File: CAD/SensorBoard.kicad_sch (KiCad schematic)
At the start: 69 parts, among them J1 USB C 2.0, J2 ARM SWD TagConnect, SW1 BOOT_SW, SW2 BOOT_SW, SW3 BOOT_SW, SW4 BOOT_SW, SW5 BOOT_SW, U1 STM32U073CCT6, U2 BME680, U3 BMI323, U4 TC1047, U5 USBLC6-2SC6, U6 MIC5365-3.3YD5, X1 32MHz, X2 32kHz768

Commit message: Add external connectors
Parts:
- removed J2: ARM SWD TagConnect, Connector:Tag-Connect_TC2030-IDC-FP_2x03_P1.27mm_Vertical, symbol Connector:Conn_ARM_SWD_TagConnect_TC2030
- removed U3: BMI323, SensorBoard:BMI323, symbol SensorBoard:BMI323
- added C20: 100n, symbol Device:C
- added J2: Conn_SWD, symbol SensorBoard:Conn_SWD
- added J3: Conn_UART, symbol SensorBoard:Conn_UART
- added J4: Conn_DAC, symbol SensorBoard:Conn_DAC
- added R26: 220, symbol Device:R
- added R27, R28, R29, R30: 100, symbol Device:R
- added SW6: BOOT_SW, symbol Switch:SW_Push
- added U5: BMI323, SensorBoard:BMI323, symbol SensorBoard:BMI323
- renumbered C11 to C1, C8 to C10, C22 to C11, C1 to C12, C2 to C13, C3 to C14, C4 to C15, C5 to C16, C6 to C17, C16 to C18, C15 to C19, C12 to C2, C14 to C21, C18 to C22, C17 to C23, C13 to C3, C19 to C4, C20 to C5, C21 to C6, C9 to C7, C10 to C8, C7 to C9, D3 to D1, D4 to D2, D5 to D3, D1 to D4, D2 to D5, R8 to R1, R16 to R10, R17 to R11, R4 to R12, R5 to R13, R18 to R14, R19 to R15, R20 to R16, R21 to R17, R1 to R18, R22 to R19, R3 to R2, R23 to R20, R24 to R21, R25 to R22, R12 to R23, R13 to R24, R11 to R25, R10 to R3, R9 to R4, R2 to R5, R7 to R6, R6 to R7, R14 to R8, R15 to R9, U5 to U1, U6 to U2, U2 to U3, U1 to U6
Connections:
- net +3V3: now also U5.5 (VDDIO), U5.8 (VDD)
- net DAC_OUT: now also J4.1 (DAC_OUT)
- net GND: now also C20.1, J2.3 (GND), J2.4 (SHIELD), J3.3 (GND), J3.4 (SHIELD), J4.2 (GND), J4.3 (SHIELD), SW6.1, U5.6 (GNDIO), U5.7 (GND)
- net IMU_INT1: now also U5.4 (INT1)
- net IMU_INT2: now also U5.9 (INT2)
- net SPI_MISO: now also U5.1 (SDO)
- net SPI_MOSI: now also U5.14 (SDX)
- net SPI_NCS: now also U5.12 (~{CSB})
- net SPI_SCK: now also U5.13 (SCX)
- net SWD_SWCLK: now also J2.1 (SWDCLK), R30.2; no longer U6.37 (PA14)
- net UART_RX: now also J3.2 (RX), R28.1; no longer U6.22 (PB11)
- net UART_TX: now also J3.1 (TX), R27.1; no longer U6.21 (PB10)
- net SWD_DWDIO renamed SWD_SWDIO_R
- net SWD_SWDIO_R: now also R29.1
- net SWD_RST renamed MCU_RST
- net MCU_RST: now also C20.2, R26.2
- net SWD_SWO: no longer names the net of U6.39 (PB3)
- new net: R26.1, SW6.2
- new net SWD_SWCLK_R: R30.1, U6.37 (PA14)
- new net SWD_SWDIO: J2.2 (SWDIO), R29.2
- new net UART_RX_R: R28.2, U6.22 (PB11)
- new net UART_TX_R: R27.2, U6.21 (PB10)
- no-connect marks 5 -> 6
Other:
- note added: "SDO (ADDR_SEL) connected to GND => I2C Address: 0x76"
- note added: "~{CSB} (PROT_SEL) connected to +3V3 => I2C Selected"
- moved on the sheet: C11, C21, C22, C23, C4, C5, C6, R14, R15, R16, R17, R19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

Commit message: Schematic clean-up
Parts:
- removed R25: 22, symbol Device:R
- added C1: 4u7, Capacitor_SMD:C_0603_1608Metric, symbol Device:C
- C10: renamed from C7; footprint (none) -> Capacitor_SMD:C_0402_1005Metric
- C11: renamed from C8; footprint (none) -> Capacitor_SMD:C_0402_1005Metric
- C12: renamed from C9; footprint (none) -> Capacitor_SMD:C_0402_1005Metric
- C13: renamed from C10; footprint (none) -> Capacitor_SMD:C_0402_1005Metric
- C14: renamed from C1; footprint (none) -> Capacitor_SMD:C_0402_1005Metric
- C15: renamed from C20; footprint (none) -> Capacitor_SMD:C_0402_1005Metric
- C16: renamed from C4; footprint (none) -> Capacitor_SMD:C_0402_1005Metric
- C17: renamed from C5; footprint (none) -> Capacitor_SMD:C_0402_1005Metric
- C18: renamed from C6; footprint (none) -> Capacitor_SMD:C_0402_1005Metric
- C19: renamed from C11; footprint (none) -> Capacitor_SMD:C_0402_1005Metric
- C2: renamed from C17; footprint (none) -> Capacitor_SMD:C_0603_1608Metric
- C20: renamed from C18; footprint (none) -> Capacitor_SMD:C_0402_1005Metric
- C21: renamed from C19; footprint (none) -> Capacitor_SMD:C_0402_1005Metric
- C22: renamed from C21; footprint (none) -> Capacitor_SMD:C_0402_1005Metric
- C23: renamed from C22; footprint (none) -> Capacitor_SMD:C_0402_1005Metric
- C24: renamed from C23; footprint (none) -> Capacitor_SMD:C_0402_1005Metric
- C3: renamed from C16; footprint (none) -> Capacitor_SMD:C_0402_1005Metric
- C4: renamed from C15; footprint (none) -> Capacitor_SMD:C_0402_1005Metric
- C5: renamed from C14; footprint (none) -> Capacitor_SMD:C_0402_1005Metric
- C6: renamed from C13; footprint (none) -> Capacitor_SMD:C_0402_1005Metric
- C7: renamed from C12; footprint (none) -> Capacitor_SMD:C_0402_1005Metric
- C8: renamed from C2; value 1u -> 4u7; footprint (none) -> Capacitor_SMD:C_0603_1608Metric
- C9: renamed from C3; value 1u -> 4u7; footprint (none) -> Capacitor_SMD:C_0603_1608Metric
- D1: renamed from D2; value LED -> RED; footprint (none) -> LED_SMD:LED_0402_1005Metric
- D2: renamed from D3; value LED -> RED; footprint (none) -> LED_SMD:LED_0402_1005Metric
- D3: renamed from D6; value LED -> RED; footprint (none) -> LED_SMD:LED_0402_1005Metric
- D4: renamed from D7; value LED -> RED; footprint (none) -> LED_SMD:LED_0402_1005Metric
- D6: renamed from D4; footprint (none) -> LED_SMD:LED_0402_1005Metric
- D7: renamed from D5; footprint (none) -> LED_SMD:LED_0402_1005Metric
- J1: footprint (none) -> Connector_USB:USB_C_Receptacle_GCT_USB4105-xx-A_16P_TopMnt_Horizontal
- J2: value Conn_SWD -> SWD Connector; footprint (none) -> Connector_Molex:Molex_PicoBlade_53048-0410_1x04_P1.25mm_Horizontal
- J3: value Conn_UART -> UART Connector; footprint (none) -> Connector_Molex:Molex_PicoBlade_53048-0410_1x04_P1.25mm_Horizontal
- J4: value Conn_DAC -> DAC Connector; footprint (none) -> Connector_Molex:Molex_PicoBlade_53261-0271_1x02-1MP_P1.25mm_Horizontal
- R1: renamed from R23; footprint (none) -> Resistor_SMD:R_0402_1005Metric
- R10: renamed from R7; footprint (none) -> Resistor_SMD:R_0402_1005Metric
- R11: renamed from R18; footprint (none) -> Resistor_SMD:R_0402_1005Metric
- R12: renamed from R2; footprint (none) -> Resistor_SMD:R_0402_1005Metric
- R13: renamed from R5; footprint (none) -> Resistor_SMD:R_0402_1005Metric
- R14: renamed from R26; footprint (none) -> Resistor_SMD:R_0402_1005Metric
- R15: renamed from R14; footprint (none) -> Resistor_SMD:R_0402_1005Metric
- R16: renamed from R15; footprint (none) -> Resistor_SMD:R_0402_1005Metric
- R17: renamed from R16; footprint (none) -> Resistor_SMD:R_0402_1005Metric
- R18: renamed from R17; footprint (none) -> Resistor_SMD:R_0402_1005Metric
- R19, R20, R21, R22: footprint (none) -> Resistor_SMD:R_0402_1005Metric
- R2: renamed from R24; footprint (none) -> Resistor_SMD:R_0402_1005Metric
- R23: renamed from R1; footprint (none) -> Resistor_SMD:R_0402_1005Metric
- R24: renamed from R3; footprint (none) -> Resistor_SMD:R_0402_1005Metric
- R25: renamed from R4; footprint (none) -> Resistor_SMD:R_0402_1005Metric
- R26: renamed from R8; footprint (none) -> Resistor_SMD:R_0402_1005Metric
- R27: renamed from R9; footprint (none) -> Resistor_SMD:R_0402_1005Metric
- R28: renamed from R10; footprint (none) -> Resistor_SMD:R_0402_1005Metric
- R29: renamed from R11; footprint (none) -> Resistor_SMD:R_0402_1005Metric
- R3: renamed from R27; footprint (none) -> Resistor_SMD:R_0402_1005Metric
- R4: renamed from R28; footprint (none) -> Resistor_SMD:R_0402_1005Metric
- R5: renamed from R29; footprint (none) -> Resistor_SMD:R_0402_1005Metric
- R6: renamed from R30; footprint (none) -> Resistor_SMD:R_0402_1005Metric
- R7: renamed from R12; footprint (none) -> Resistor_SMD:R_0402_1005Metric
- R8: renamed from R13; footprint (none) -> Resistor_SMD:R_0402_1005Metric
- R9: renamed from R6; footprint (none) -> Resistor_SMD:R_0402_1005Metric
- SW1: renamed from SW2; value BOOT_SW -> SW_1; footprint (none) -> Button_Switch_SMD:SW_Push_SPST_NO_Alps_SKRK
- SW2: renamed from SW3; value BOOT_SW -> SW_2; footprint (none) -> Button_Switch_SMD:SW_Push_SPST_NO_Alps_SKRK
- SW3: renamed from SW4; value BOOT_SW -> SW_3; footprint (none) -> Button_Switch_SMD:SW_Push_SPST_NO_Alps_SKRK
- SW4: renamed from SW5; value BOOT_SW -> SW_4; footprint (none) -> Button_Switch_SMD:SW_Push_SPST_NO_Alps_SKRK
- SW5: renamed from SW1; value BOOT_SW -> SW_BOOT; footprint (none) -> Button_Switch_SMD:SW_Push_SPST_NO_Alps_SKRK
- SW6: value BOOT_SW -> SW_RST; footprint (none) -> Button_Switch_SMD:SW_Push_SPST_NO_Alps_SKRK
- U2: value MIC5365-3.3YD5 -> MIC5365
- U6: renamed from U4; symbol Sensor_Temperature:TC1047xNB -> SensorBoard:TC1047
- X1: footprint (none) -> Crystal:Crystal_SMD_2016-4Pin_2.0x1.6mm
- X2: footprint (none) -> Crystal:Crystal_SMD_2012-2Pin_2.0x1.2mm
- renumbered D1 to D5, U6 to U1, U1 to U3, U3 to U4
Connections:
- net SPI_SCK_R is gone; now on net SPI_SCK: U1.26 (PB13)
- net +3V3: now also C1.2
- net GND: now also C1.1
- net LED_4_R: now reaches D4.2 (A), R29.2
- net HSE_OUT_R: now reaches C11.1, R11.1, X1.3
- net LED_2_R: now reaches D2.2 (A), R27.2
- net LED_R_R: now reaches D5.5 (AR), R24.2
- net BTN_3_R: now reaches R19.1, SW3.2
- net LED_G_R: now reaches D5.4 (AG), R23.2
- net LED_3_R: now reaches D3.2 (A), R28.2
- net LED_1_R: now reaches D1.2 (A), R26.2
- net MCU_BOOT_R: now reaches R12.1, SW5.2
- net LED_B_R: now reaches D5.6 (AB), R25.2
- net BTN_4_R: now reaches R21.1, SW4.2
- net MCU_RST_R: now reaches R14.1, SW6.2
- net BTN_2_R: now reaches R17.1, SW2.2
- net BTN_1_R: now reaches R15.1, SW1.2
- net BOOT renamed MCU_BOOT
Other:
- note added: "+5V and +3V3 Debug LEDs"
- note added: "Analogue Temperature Sensor"
- note added: "BOOT and ~{RESET} Buttons"
- note added: "External DAC Connector"
- note added: "External SWD Connector"
- note added: "External UART Connector"
- note added: "High-Speed External Crystal Oscillatror (32MHz)"
- note added: "Humidity, Pressure, Temperature, and Volatile Organic Compounds Sensor on I^{2}C"
- note added: "Inertial Measurement Unit on SPI"
- note added: "Low-Speed External Crystal Oscillatror (32Hz768)"
- note added: "RGB and 4 Red LEDs"
- note added: "SDO (ADDR_SEL) connected to GND => I^{2}C Address: 0x76"
- note added: "USB Type-C 2.0 Connector with ESD Protection"
- note added: "Ultra-Low Power Microcontroller - STM32U073"
- note added: "User buttons"
- note added: "~{CSB} (PROT_SEL) connected to +3V3 => I^{2}C Selected"
- note removed: "SDO (ADDR_SEL) connected to GND => I2C Address: 0x76"
- note removed: "~{CSB} (PROT_SEL) connected to +3V3 => I2C Selected"
- moved on the sheet: C10, C11, C12, C13, C14, C15, C16, C17, C18, C19, C2, C20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

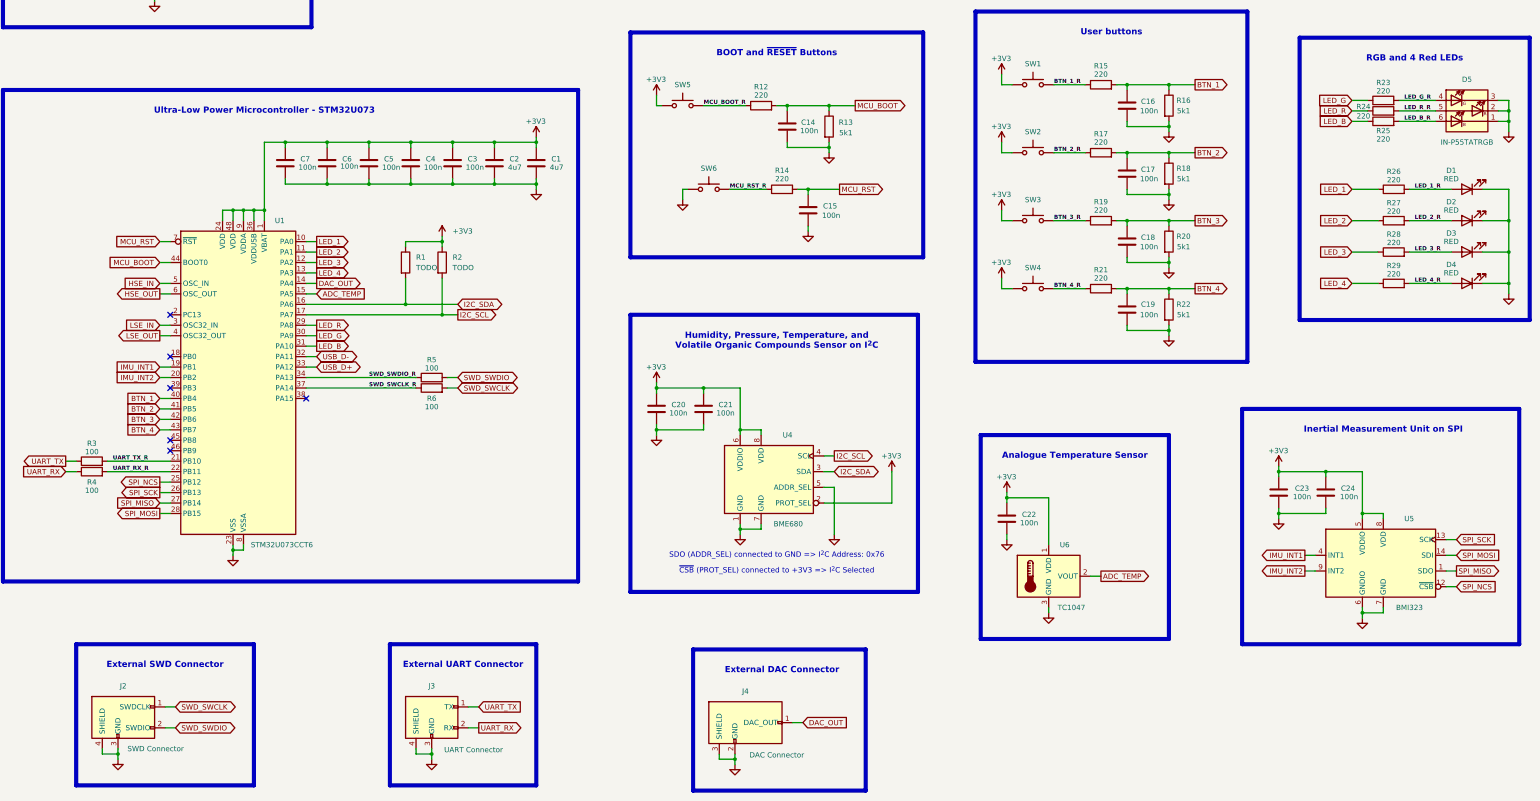
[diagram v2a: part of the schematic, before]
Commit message: Update connector footprints and RGB LED
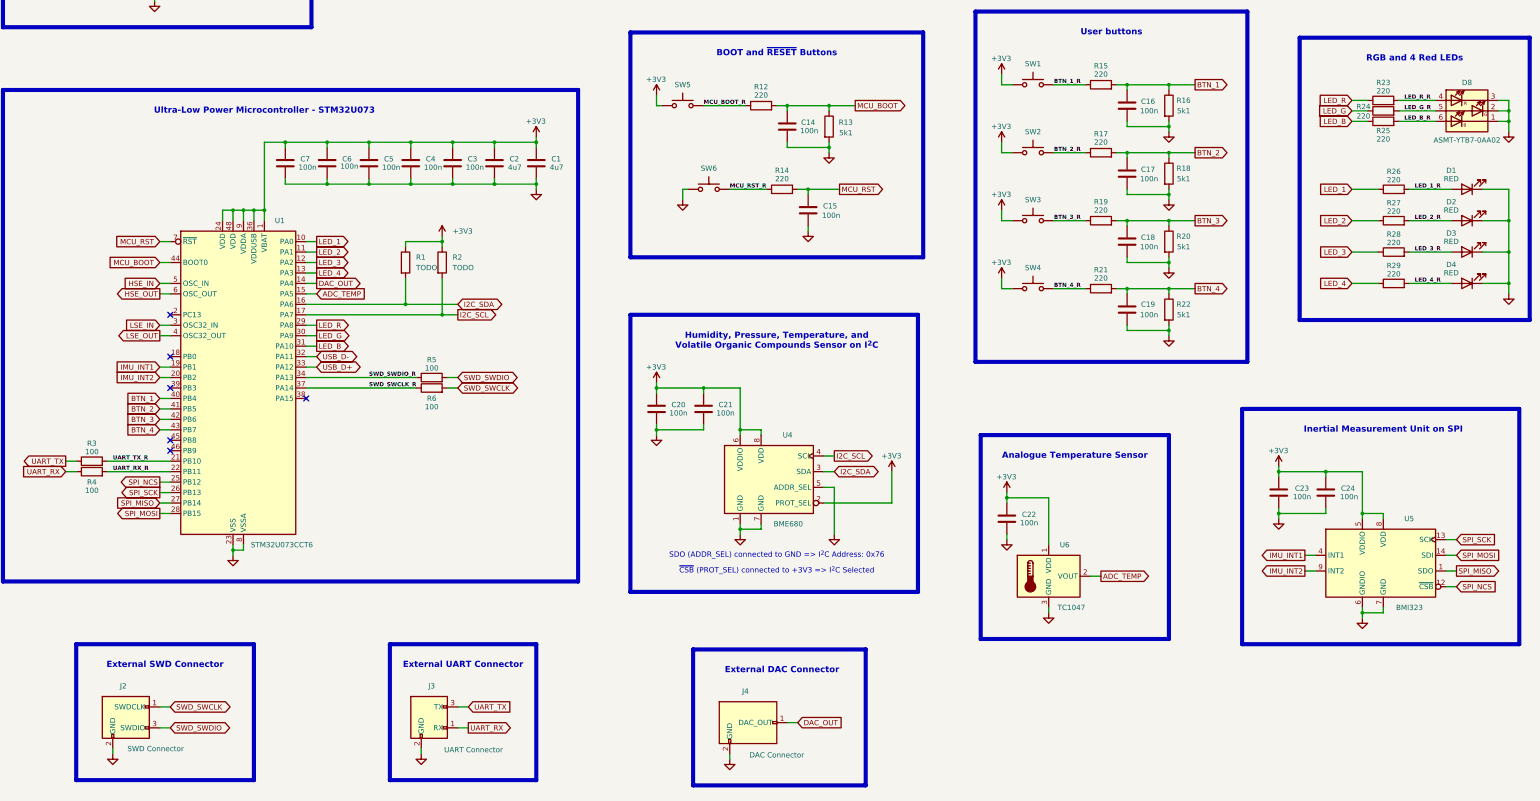
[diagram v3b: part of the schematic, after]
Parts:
- removed D5: IN-P55TATRGB, LED_SMD:LED_Inolux_IN-P55TATRGB_PLCC6_5.0x5.5mm_P1.8mm, symbol LED:Inolux_IN-P55TATRGB
- added D8: ASMT-YTB7-0AA02, LED_SMD:LED_Avago_PLCC6_3x2.8mm, symbol LED:ASMT-YTB7-0AA02
- J2, J3: footprint Connector_Molex:Molex_PicoBlade_53048-0410_1x04_P1.25mm_Horizontal -> SensorBoard:SM03B-SR
- J4: footprint Connector_Molex:Molex_PicoBlade_53261-0271_1x02-1MP_P1.25mm_Horizontal -> SensorBoard:SM02B-SR
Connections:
- net GND: now also J2.2 (GND), J3.2 (GND), D8.1 (KB), D8.2 (KG), D8.3 (KR); no longer J2.3 (GND), J2.4 (SHIELD), J3.3 (GND), J3.4 (SHIELD), J4.3 (SHIELD)
- net LED_B_R: now also D8.6 (AB)
- net LED_G: now also R24.1; no longer R23.1
- net LED_G_R: now also R24.2, D8.5 (AG); no longer R23.2
- net LED_R: now also R23.1; no longer R24.1
- net LED_R_R: now also R23.2, D8.4 (AR); no longer R24.2
- net SWD_SWDIO: now also J2.3 (SWDIO); no longer J2.2 (SWDIO)
- net UART_RX: now also J3.1 (RX); no longer J3.2 (RX)
- net UART_TX: now also J3.3 (TX); no longer J3.1 (TX)

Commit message: Begin initial PCB design
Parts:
- added M1: M1, MountingHole:MountingHole_3.2mm_M3_Pad_Via, symbol Mechanical:MountingHole_Pad
- added M2: M2, MountingHole:MountingHole_3.2mm_M3_Pad_Via, symbol Mechanical:MountingHole_Pad
- added M3: M3, MountingHole:MountingHole_3.2mm_M3_Pad_Via, symbol Mechanical:MountingHole_Pad
- added M4: M4, MountingHole:MountingHole_3.2mm_M3_Pad_Via, symbol Mechanical:MountingHole_Pad
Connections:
- net GND: now also M1.1, M2.1, M3.1, M4.1
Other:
- note added: "Mounting Holes"
- moved on the sheet: J2, J3, J4

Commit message: Add updates to footprints
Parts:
- M1, M2, M3, M4: symbol Mechanical:MountingHole_Pad -> Mechanical:MountingHole
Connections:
- net GND: no longer M1.1, M2.1, M3.1, M4.1

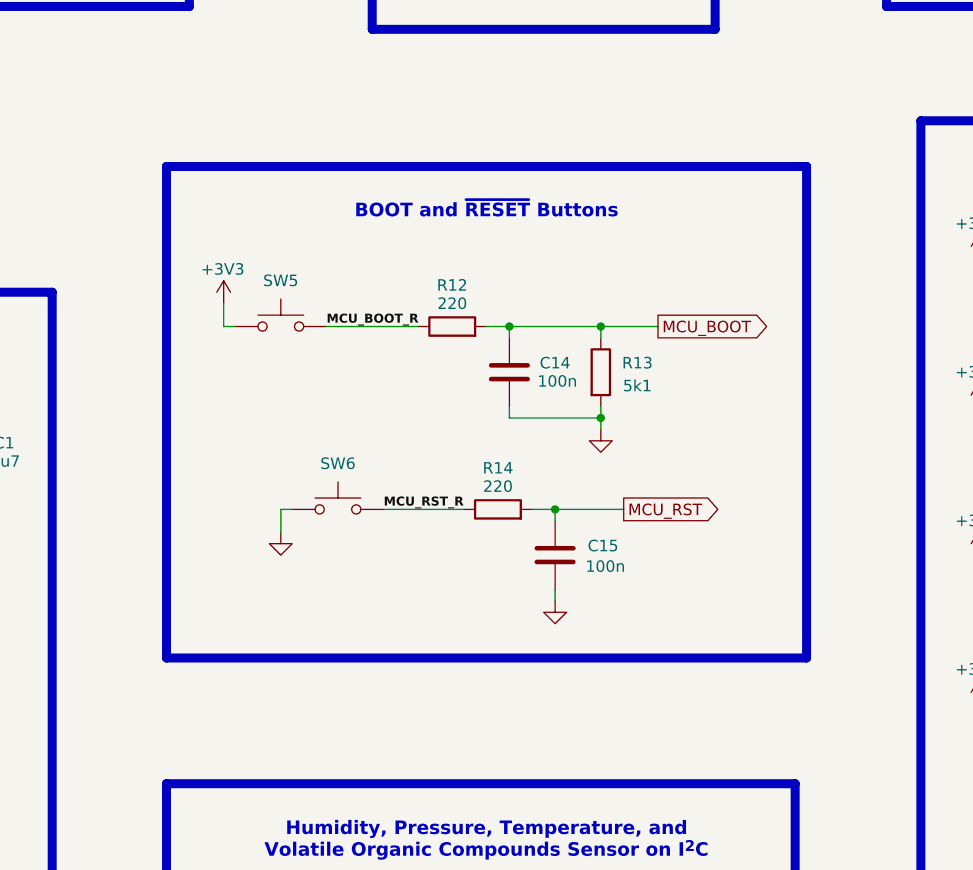
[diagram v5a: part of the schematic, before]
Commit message: Update and add more footprints
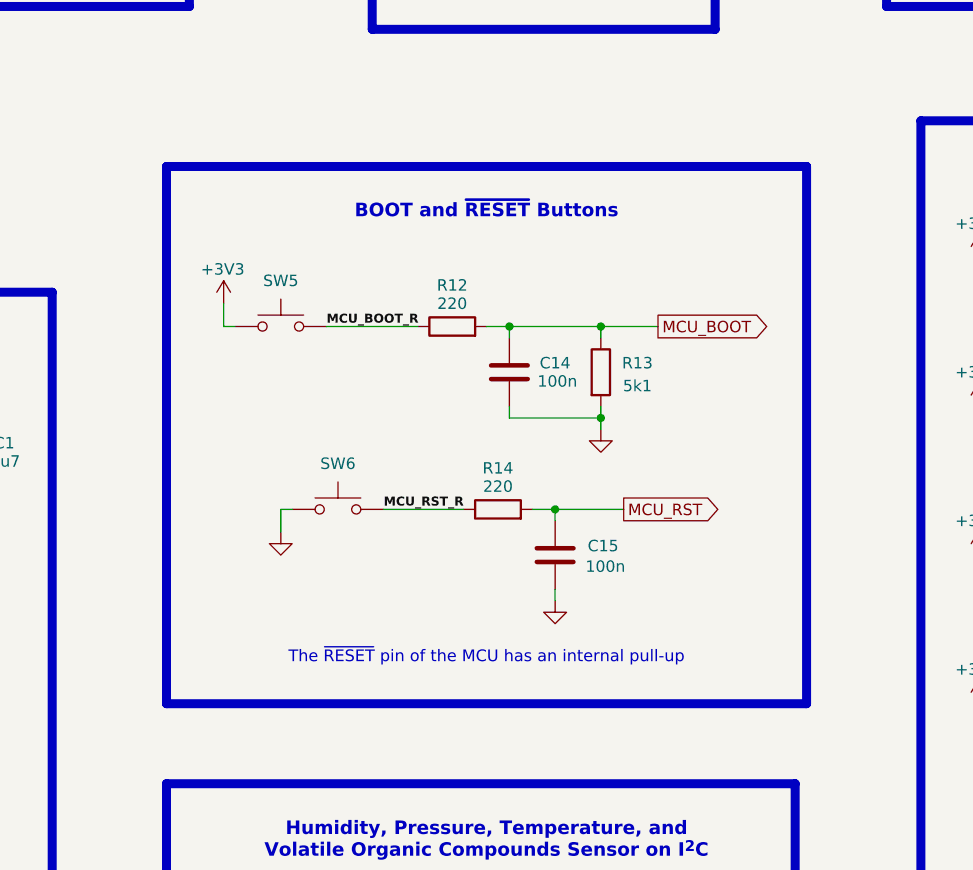
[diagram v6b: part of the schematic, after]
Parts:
- D1, D2, D3, D4, D6, D7: footprint LED_SMD:LED_0402_1005Metric -> LED_SMD:LED_0805_2012Metric
- D8: footprint LED_SMD:LED_Avago_PLCC6_3x2.8mm -> SensorBoard:ASMT-YTB7-0AA02
- SW1, SW2, SW3, SW4, SW5, SW6: footprint Button_Switch_SMD:SW_Push_SPST_NO_Alps_SKRK -> SensorBoard:PTS636-SM25F-SMTR-LFS
- U1: footprint Package_QFP:LQFP-48_7x7mm_P0.5mm -> SensorBoard:LQFP-48_7x7mm_P0.5mm
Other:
- note added: "The ~{RESET} pin of the MCU has an internal pull-up"
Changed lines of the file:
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@@
 	(rectangle
 		(start 176.53 90.17)
-		(end 247.65 144.78)
+		(end 247.65 149.86)
 		(stroke
 			(width 1)
@@
 		)
 	)
+	(text "The ~{RESET} pin of the MCU has an internal pull-up"
+		(exclude_from_sim yes)
+		(at 212.09 144.78 0)
+		(effects
+			(font
+				(size 1.3 1.3)
+			)
+		)
+	)
 	(text "User buttons"
 		(exclude_from_sim no)
@@
 			)
 		)
-		(property "Footprint" "Button_Switch_SMD:SW_Push_SPST_NO_Alps_SKRK"
+		(property "Footprint" "SensorBoard:PTS636-SM25F-SMTR-LFS"
 			(at 274.32 130.81 0)
 			(effects
@@
 			)
 		)
-		(property "Footprint" "LED_SMD:LED_0402_1005Metric"
+		(property "Footprint" "LED_SMD:LED_0805_2012Metric"
 			(at 379.73 143.51 0)
 			(effects
@@
 			)
 		)
-		(property "Footprint" "LED_SMD:LED_0402_1005Metric"
+		(property "Footprint" "LED_SMD:LED_0805_2012Metric"
 			(at 379.73 128.27 0)
 			(effects
@@
 			)
 		)
-		(property "Footprint" "Button_Switch_SMD:SW_Push_SPST_NO_Alps_SKRK"
+		(property "Footprint" "SensorBoard:PTS636-SM25F-SMTR-LFS"
 			(at 274.32 147.32 0)
 			(effects
@@
 			)
 		)
-		(property "Footprint" "Button_Switch_SMD:SW_Push_SPST_NO_Alps_SKRK"
+		(property "Footprint" "SensorBoard:PTS636-SM25F-SMTR-LFS"
 			(at 195.58 123.19 0)
 			(effects
@@
 			)
 		)
-		(property "Footprint" "LED_SMD:LED_0402_1005Metric"
+		(property "Footprint" "LED_SMD:LED_0805_2012Metric"
 			(at 379.73 151.13 0)
 			(effects
@@
 			)
 		)
-		(property "Footprint" "Button_Switch_SMD:SW_Push_SPST_NO_Alps_SKRK"
+		(property "Footprint" "SensorBoard:PTS636-SM25F-SMTR-LFS"
 			(at 274.32 114.3 0)
 			(effects
@@
 			)
 		)
-		(property "Footprint" "LED_SMD:LED_0402_1005Metric"
+		(property "Footprint" "LED_SMD:LED_0805_2012Metric"
 			(at 379.73 135.89 0)
 			(effects
@@
 			)
 		)
-		(property "Footprint" "LED_SMD:LED_0402_1005Metric"
+		(property "Footprint" "LED_SMD:LED_0805_2012Metric"
 			(at 224.79 62.23 0)
 			(effects
@@
 			)
 		)
-		(property "Footprint" "Button_Switch_SMD:SW_Push_SPST_NO_Alps_SKRK"
+		(property "Footprint" "SensorBoard:PTS636-SM25F-SMTR-LFS"
 			(at 274.32 97.79 0)
 			(effects
@@
 			)
 		)
-		(property "Footprint" "LED_SMD:LED_Avago_PLCC6_3x2.8mm"
+		(property "Footprint" "SensorBoard:ASMT-YTB7-0AA02"
 			(at 374.65 117.348 0)
 			(effects
@@
 			)
 		)
-		(property "Footprint" "LED_SMD:LED_0402_1005Metric"
+		(property "Footprint" "LED_SMD:LED_0805_2012Metric"
 			(at 209.55 62.23 0)
 			(effects
@@
 			)
 		)
-		(property "Footprint" "Package_QFP:LQFP-48_7x7mm_P0.5mm"
+		(property "Footprint" "SensorBoard:LQFP-48_7x7mm_P0.5mm"
 			(at 67.31 212.09 0)
 			(effects
@@
 			)
 		)
-		(property "Footprint" "Button_Switch_SMD:SW_Push_SPST_NO_Alps_SKRK"
+		(property "Footprint" "SensorBoard:PTS636-SM25F-SMTR-LFS"
 			(at 189.23 102.87 0)
 			(effects
